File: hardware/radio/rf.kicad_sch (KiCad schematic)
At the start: 40 parts, among them J1 SMA-KE-347-H13.5-1.6, U1 CC1101RGPR, X1 X322526MMB4SI

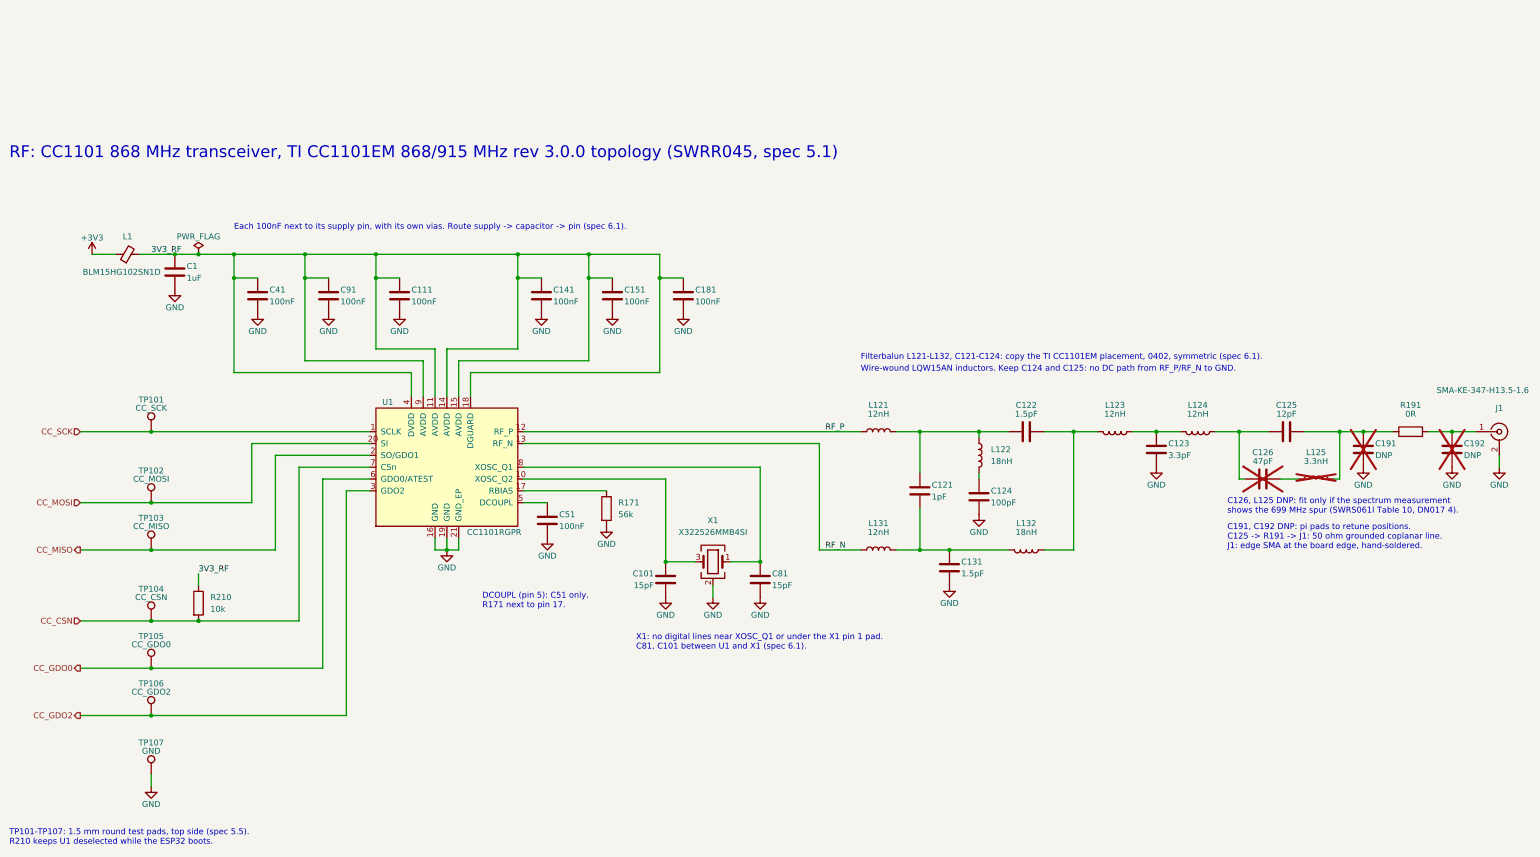
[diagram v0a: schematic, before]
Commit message: feat(hardware): move the radio to the ebyte e07 module and fix the power review findings
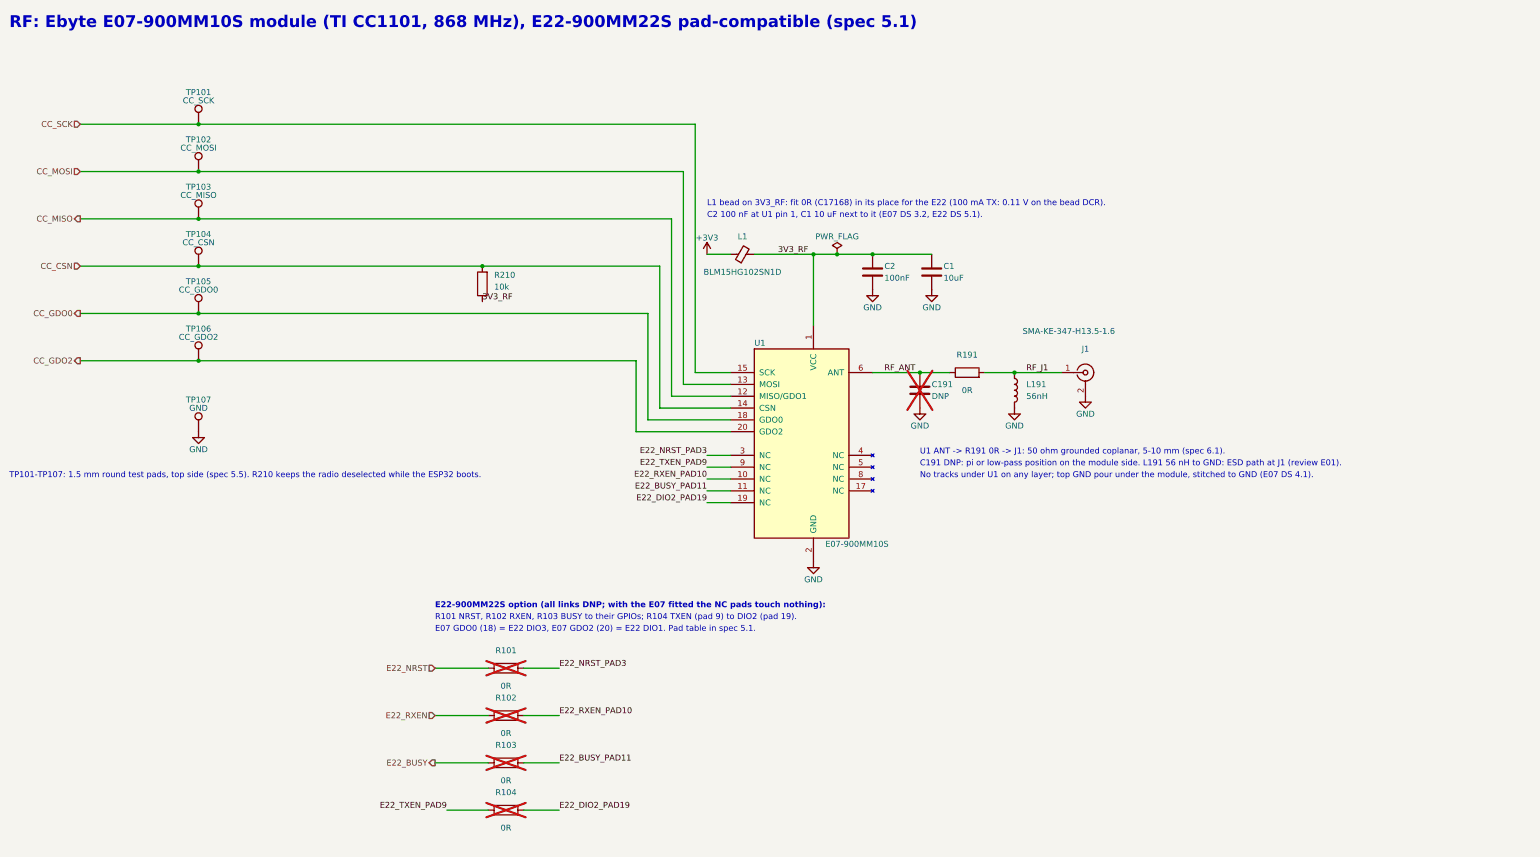
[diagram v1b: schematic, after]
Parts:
- removed C101, C81: 15pF, freedo-radio:C_0402_1005Metric, symbol freedo-radio:C
- removed C111, C141, C151, C181, C41, C51, C91: 100nF, freedo-radio:C_0402_1005Metric, symbol freedo-radio:C
- removed C121: 1pF, freedo-radio:C_0402_1005Metric, symbol freedo-radio:C
- removed C122, C131: 1.5pF, freedo-radio:C_0402_1005Metric, symbol freedo-radio:C
- removed C123: 3.3pF, freedo-radio:C_0402_1005Metric, symbol freedo-radio:C
- removed C124: 100pF, freedo-radio:C_0402_1005Metric, symbol freedo-radio:C
- removed C125: 12pF, freedo-radio:C_0402_1005Metric, symbol freedo-radio:C
- removed C126: 47pF, freedo-radio:C_0402_1005Metric, symbol freedo-radio:C
- removed C192: DNP, freedo-radio:C_0402_1005Metric, symbol freedo-radio:C
- removed L121, L123, L124, L131: 12nH, freedo-radio:L_0402_1005Metric, symbol freedo-radio:L
- removed L122, L132: 18nH, freedo-radio:L_0402_1005Metric, symbol freedo-radio:L
- removed L125: 3.3nH, freedo-radio:L_0402_1005Metric, symbol freedo-radio:L
- removed R171: 56k, freedo-radio:R_0402_1005Metric, symbol freedo-radio:R
- removed U1: CC1101RGPR, freedo-radio:QFN-20-1EP_4x4mm_P0.5mm_EP2.4x2.4mm_TI_RGP0020H, symbol freedo-radio:CC1101RGPR
- removed X1: X322526MMB4SI, freedo-radio:CRYSTAL-SMD_4P-L3.2-W2.5-BL, symbol freedo-radio:X322526MMB4SI
- added C2: 100nF, freedo-radio:C_0603_1608Metric, symbol freedo-radio:C
- added L191: 56nH, freedo-radio:L_0402_1005Metric, symbol freedo-radio:L
- added R101, R102, R103, R104: 0R, freedo-radio:R_0603_1608Metric, symbol freedo-radio:R
- added U1: E07-900MM10S, freedo-radio:Ebyte_LCC-20_10x10mm_P1.27mm_E07-MM10S_E22-MM22S, symbol freedo-radio:E07-900MM10S
- C1: value 1uF -> 10uF; footprint freedo-radio:C_0402_1005Metric -> freedo-radio:C_0603_1608Metric; LCSC C52923 -> C19702; MPN CL05A105KA5NQNC -> CL10A106KP8NNNC
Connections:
- net 3V3_RF: now also C2.1, U1.1 (VCC)
- net CC_CSN: now also U1.14 (CSN)
- net CC_GDO0: now also U1.18 (GDO0)
- net CC_GDO2: now also U1.20 (GDO2)
- net CC_MISO: now also U1.12 (MISO/GDO1)
- net CC_MOSI: now also U1.13 (MOSI)
- net CC_SCK: now also U1.15 (SCK)
- net GND: now also C2.2, L191.2, U1.16 (GND), U1.2 (GND), U1.7 (GND)
- net RF_ANT: now reaches C191.1, R191.1
- net RF_ANT: now also U1.6 (ANT)
- net RF_J1: now reaches J1.1 (In), R191.2
- net RF_J1: now also L191.1
- new net E22_BUSY: R103.1
- new net E22_BUSY_PAD11: R103.2, U1.11 (NC)
- new net E22_DIO2_PAD19: R104.2, U1.19 (NC)
- new net E22_NRST: R101.1
- new net E22_NRST_PAD3: R101.2, U1.3 (NC)
- new net E22_RXEN: R102.1
- new net E22_RXEN_PAD10: R102.2, U1.10 (NC)
- new net E22_TXEN_PAD9: R104.1, U1.9 (NC)
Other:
- note added: "C191 DNP: pi or low-pass position on the module side. L191 56 nH to GND: ESD path at J1 (review E01)."
- note added: "C2 100 nF at U1 pin 1, C1 10 uF next to it (E07 DS 3.2, E22 DS 5.1)."
- note added: "E07 GDO0 (18) = E22 DIO3, E07 GDO2 (20) = E22 DIO1. Pad table in spec 5.1."
- note added: "E22-900MM22S option (all links DNP; with the E07 fitted the NC pads touch nothing):"
- note added: "L1 bead on 3V3_RF: fit 0R (C17168) in its place for the E22 (100 mA TX: 0.11 V on the bead DCR)."
- note added: "No tracks under U1 on any layer; top GND pour under the module, stitched to GND (E07 DS 4.1)."
- note added: "R101 NRST, R102 RXEN, R103 BUSY to their GPIOs; R104 TXEN (pad 9) to DIO2 (pad 19)."
- note added: "RF: Ebyte E07-900MM10S module (TI CC1101, 868 MHz), E22-900MM22S pad-compatible (spec 5.1)"
- note added: "TP101-TP107: 1.5 mm round test pads, top side (spec 5.5). R210 keeps the radio deselected while the ESP32 boots."
- note added: "U1 ANT -> R191 0R -> J1: 50 ohm grounded coplanar, 5-10 mm (spec 6.1)."
- note removed: "C126, L125 DNP: fit only if the spectrum measurement shows the 699 MHz spur (SWRS061I Table 10, DN017 4)."
- note removed: "C191, C192 DNP: pi pads to retune positions. C125 -> R191 -> J1: 50 ohm grounded coplanar line. J1: edge SMA at the board edge, hand-soldered."
- note removed: "DCOUPL (pin 5): C51 only. R171 next to pin 17."
- note removed: "Each 100nF next to its supply pin, with its own vias. Route supply -> capacitor -> pin (spec 6.1)."
- note removed: "Filterbalun L121-L132, C121-C124: copy the TI CC1101EM placement, 0402, symmetric (spec 6.1)."
- note removed: "RF: CC1101 868 MHz transceiver, TI CC1101EM 868/915 MHz rev 3.0.0 topology (SWRR045, spec 5.1)"
- note removed: "TP101-TP107: 1.5 mm round test pads, top side (spec 5.5). R210 keeps U1 deselected while the ESP32 boots."
- note removed: "Wire-wound LQW15AN inductors. Keep C124 and C125: no DC path from RF_P/RF_N to GND."
- note removed: "X1: no digital lines near XOSC_Q1 or under the X1 pin 1 pad. C81, C101 between U1 and X1 (spec 6.1)."
- title: freedo radio rev A: RF, CC1101 868 MHz -> freedo radio rev A: RF, E07-900MM10S 868 MHz

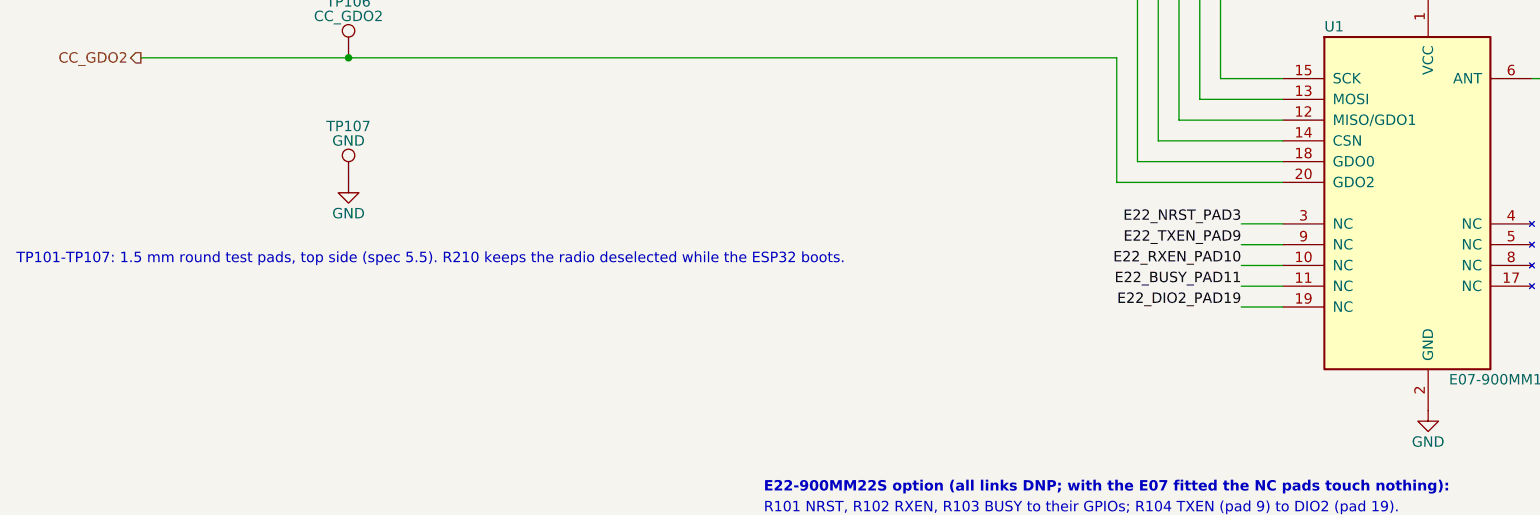
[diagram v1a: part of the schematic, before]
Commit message: fix(hardware): apply the routed-board review fixes
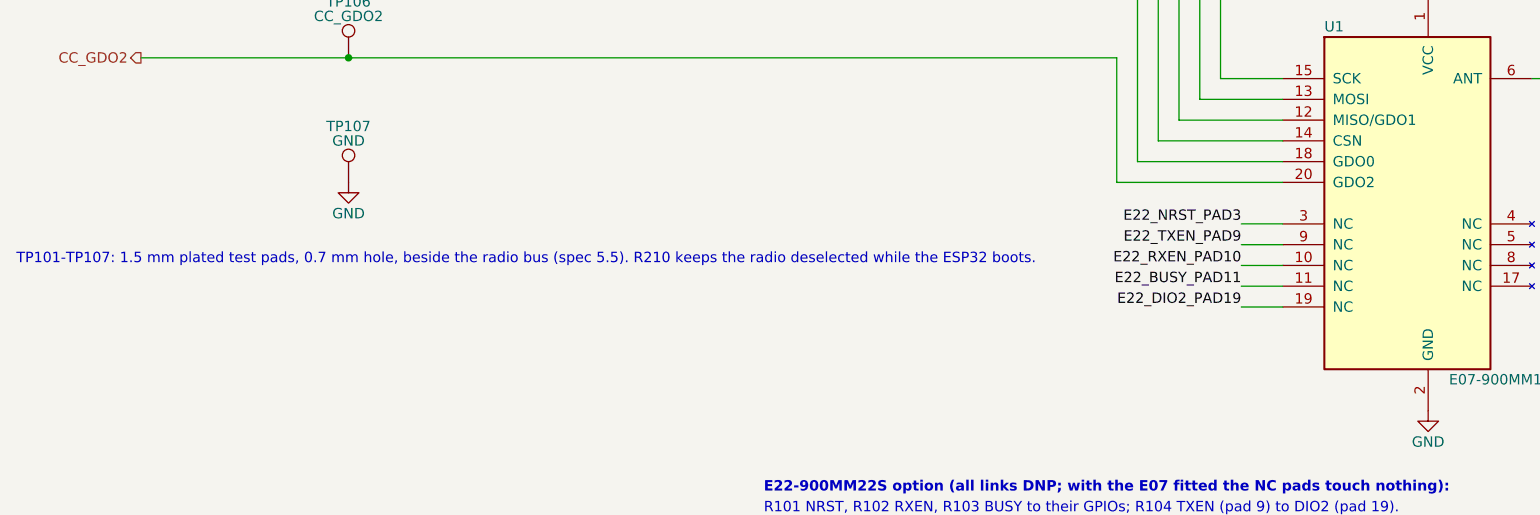
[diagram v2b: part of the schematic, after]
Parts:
- TP101, TP102, TP103, TP104, TP105, TP106, TP107: footprint freedo-radio:TestPoint_Pad_D1.5mm -> freedo-radio:TestPoint_THTPad_D1.5mm_Drill0.7mm
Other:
- note added: "TP101-TP107: 1.5 mm plated test pads, 0.7 mm hole, beside the radio bus (spec 5.5). R210 keeps the radio deselected while the ESP32 boots."
- note removed: "TP101-TP107: 1.5 mm round test pads, top side (spec 5.5). R210 keeps the radio deselected while the ESP32 boots."
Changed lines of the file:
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@@
 			)
 		)
-		(property "Footprint" "freedo-radio:TestPoint_Pad_D1.5mm"
+		(property "Footprint" "freedo-radio:TestPoint_THTPad_D1.5mm_Drill0.7mm"
 			(at 99.06 71.12 0)
 			(hide yes)
@@
 			)
 		)
-		(property "Footprint" "freedo-radio:TestPoint_Pad_D1.5mm"
+		(property "Footprint" "freedo-radio:TestPoint_THTPad_D1.5mm_Drill0.7mm"
 			(at 99.06 81.28 0)
 			(hide yes)
@@
 			)
 		)
-		(property "Footprint" "freedo-radio:TestPoint_Pad_D1.5mm"
+		(property "Footprint" "freedo-radio:TestPoint_THTPad_D1.5mm_Drill0.7mm"
 			(at 99.06 91.44 0)
 			(hide yes)
@@
 			)
 		)
-		(property "Footprint" "freedo-radio:TestPoint_Pad_D1.5mm"
+		(property "Footprint" "freedo-radio:TestPoint_THTPad_D1.5mm_Drill0.7mm"
 			(at 99.06 101.6 0)
 			(hide yes)
@@
 			)
 		)
-		(property "Footprint" "freedo-radio:TestPoint_Pad_D1.5mm"
+		(property "Footprint" "freedo-radio:TestPoint_THTPad_D1.5mm_Drill0.7mm"
 			(at 99.06 111.76 0)
 			(hide yes)
@@
 			)
 		)
-		(property "Footprint" "freedo-radio:TestPoint_Pad_D1.5mm"
+		(property "Footprint" "freedo-radio:TestPoint_THTPad_D1.5mm_Drill0.7mm"
 			(at 99.06 121.92 0)
 			(hide yes)
@@
 			)
 		)
-		(property "Footprint" "freedo-radio:TestPoint_Pad_D1.5mm"
+		(property "Footprint" "freedo-radio:TestPoint_THTPad_D1.5mm_Drill0.7mm"
 			(at 99.06 137.16 0)
 			(hide yes)
@@
 		)
 	)
-	(text "TP101-TP107: 1.5 mm round test pads, top side (spec 5.5). R210 keeps the radio deselected while the ESP32 boots."
+	(text "TP101-TP107: 1.5 mm plated test pads, 0.7 mm hole, beside the radio bus (spec 5.5). R210 keeps the radio deselected while the ESP32 boots."
 		(exclude_from_sim no)
 		(at 58.42 147.32 0)
